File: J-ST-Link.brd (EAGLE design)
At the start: 35.6 x 25.4 mm, 17 parts, among them IC1 TLV70433

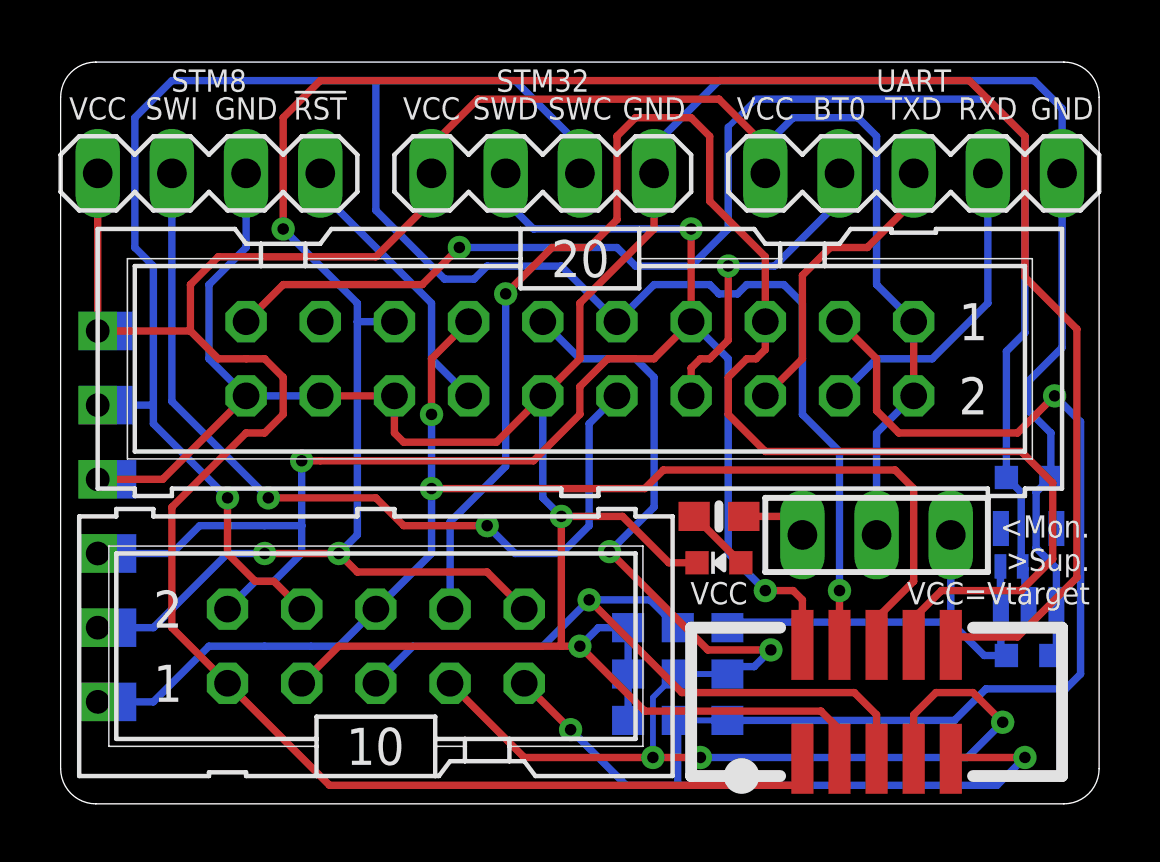
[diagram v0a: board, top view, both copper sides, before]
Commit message: Optimised routing
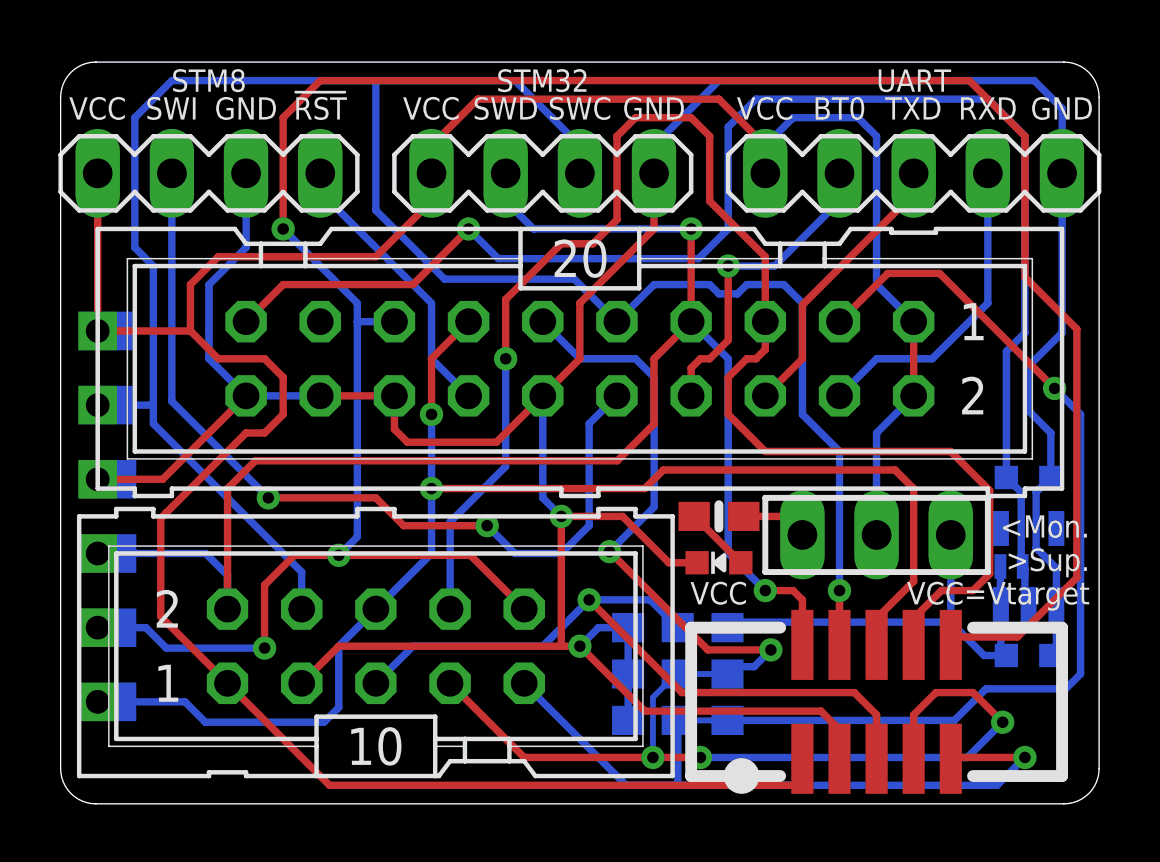
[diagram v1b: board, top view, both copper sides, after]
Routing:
- net TDI: track 55.2 -> 51.0 mm
- net !RESET: track 82.0 -> 83.8 mm
- net SWO/TDO: track 44.9 -> 46.7 mm
- net UART_TX: track 10.5 -> 9.72 mm
- net SWCLK/TCK: track 73.4 -> 72.6 mm, vias 2 -> 1
- net !TRST: track 33.2 -> 32.6 mm
- net SWDIO/TMS: track 53.8 -> 53.7 mm, vias 3 -> 2
- net TRST/NC/GND: vias 2 -> 1

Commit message: Optimised schematic
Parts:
- R1: value 1K -> 330R
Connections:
- net SWIM_RST renamed !SWIM_RST
- net VTREF renamed VCC
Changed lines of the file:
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@@
 <grid distance="0.127" unitdist="mm" unit="mm" style="dots" multiple="4" display="yes" altdistance="1" altunitdist="mil" altunit="mil"/>
 <layers>
-<layer number="1" name="Top" color="4" fill="1" visible="yes" active="yes"/>
-<layer number="16" name="Bottom" color="1" fill="1" visible="yes" active="yes"/>
-<layer number="17" name="Pads" color="2" fill="1" visible="yes" active="yes"/>
-<layer number="18" name="Vias" color="2" fill="1" visible="yes" active="yes"/>
+<layer number="1" name="Top" color="4" fill="1" visible="no" active="yes"/>
+<layer number="16" name="Bottom" color="1" fill="1" visible="no" active="yes"/>
+<layer number="17" name="Pads" color="2" fill="1" visible="no" active="yes"/>
+<layer number="18" name="Vias" color="2" fill="1" visible="no" active="yes"/>
 <layer number="19" name="Unrouted" color="6" fill="1" visible="yes" active="yes"/>
 <layer number="20" name="Dimension" color="24" fill="1" visible="yes" active="yes"/>
 <layer number="21" name="tPlace" color="7" fill="1" visible="yes" active="yes"/>
-<layer number="22" name="bPlace" color="7" fill="1" visible="yes" active="yes"/>
+<layer number="22" name="bPlace" color="7" fill="1" visible="no" active="yes"/>
 <layer number="23" name="tOrigins" color="15" fill="1" visible="yes" active="yes"/>
-<layer number="24" name="bOrigins" color="15" fill="1" visible="yes" active="yes"/>
+<layer number="24" name="bOrigins" color="15" fill="1" visible="no" active="yes"/>
 <layer number="25" name="tNames" color="7" fill="1" visible="yes" active="yes"/>
-<layer number="26" name="bNames" color="7" fill="1" visible="yes" active="yes"/>
-<layer number="27" name="tValues" color="7" fill="1" visible="yes" active="yes"/>
-<layer number="28" name="bValues" color="7" fill="1" visible="yes" active="yes"/>
-<layer number="29" name="tStop" color="7" fill="3" visible="no" active="yes"/>
+<layer number="26" name="bNames" color="7" fill="1" visible="no" active="yes"/>
+<layer number="27" name="tValues" color="7" fill="1" visible="no" active="yes"/>
+<layer number="28" name="bValues" color="7" fill="1" visible="no" active="yes"/>
+<layer number="29" name="tStop" color="7" fill="3" visible="yes" active="yes"/>
 <layer number="30" name="bStop" color="7" fill="6" visible="no" active="yes"/>
 <layer number="31" name="tCream" color="7" fill="4" visible="no" active="yes"/>
@@
 <layer number="37" name="tTest" color="7" fill="1" visible="no" active="yes"/>
 <layer number="38" name="bTest" color="7" fill="1" visible="no" active="yes"/>
-<layer number="39" name="tKeepout" color="4" fill="11" visible="yes" active="yes"/>
-<layer number="40" name="bKeepout" color="1" fill="11" visible="yes" active="yes"/>
-<layer number="41" name="tRestrict" color="4" fill="10" visible="yes" active="yes"/>
-<layer number="42" name="bRestrict" color="1" fill="10" visible="yes" active="yes"/>
-<layer number="43" name="vRestrict" color="2" fill="10" visible="yes" active="yes"/>
+<layer number="39" name="tKeepout" color="4" fill="11" visible="no" active="yes"/>
+<layer number="40" name="bKeepout" color="1" fill="11" visible="no" active="yes"/>
+<layer number="41" name="tRestrict" color="4" fill="10" visible="no" active="yes"/>
+<layer number="42" name="bRestrict" color="1" fill="10" visible="no" active="yes"/>
+<layer number="43" name="vRestrict" color="2" fill="10" visible="no" active="yes"/>
 <layer number="44" name="Drills" color="7" fill="1" visible="no" active="yes"/>
-<layer number="45" name="Holes" color="7" fill="1" visible="no" active="yes"/>
-<layer number="46" name="Milling" color="3" fill="1" visible="no" active="yes"/>
-<layer number="47" name="Measures" color="7" fill="1" visible="no" active="yes"/>
+<layer number="45" name="Holes" color="7" fill="1" visible="yes" active="yes"/>
+<layer number="46" name="Milling" color="3" fill="1" visible="yes" active="yes"/>
+<layer number="47" name="Measures" color="7" fill="1" visible="yes" active="yes"/>
 <layer number="48" name="Document" color="7" fill="1" visible="yes" active="yes"/>
 <layer number="49" name="Reference" color="7" fill="1" visible="yes" active="yes"/>
-<layer number="51" name="tDocu" color="7" fill="1" visible="yes" active="yes"/>
-<layer number="52" name="bDocu" color="7" fill="1" visible="yes" active="yes"/>
+<layer number="51" name="tDocu" color="7" fill="1" visible="no" active="yes"/>
+<layer number="52" name="bDocu" color="7" fill="1" visible="no" active="yes"/>
 <layer number="88" name="SimResults" color="9" fill="1" visible="no" active="no"/>
 <layer number="89" name="SimProbes" color="9" fill="1" visible="no" active="no"/>
@@
 </element>
 <element name="10-127" library="Progger2 (3)" package="CON-HARTING-ML_ML10S" value="" x="27.94" y="3.4925" smashed="yes"/>
-<element name="R1" library="microbuilder" package="0603-NO" value="1K" x="22.5425" y="9.8425" smashed="yes"/>
+<element name="R1" library="microbuilder" package="0603-NO" value="330R" x="22.5425" y="9.8425" smashed="yes"/>
 <element name="LED1" library="microbuilder" package="CHIPLED_0603_NOOUTLINE" value="" x="22.5425" y="8.255" smashed="yes" rot="R90">
 <attribute name="VALUE" x="24.5425" y="7.255" size="1.27" layer="27" rot="R90"/>
@@
 </elements>
 <signals>
-<signal name="VTREF">
+<signal name="VCC">
 <contactref element="J-/ST-LINK" pad="1"/>
 <contactref element="J-/ST-LINK" pad="2"/>
@@
 <wire x1="10.795" y1="10.4775" x2="7.112" y2="10.4775" width="0.254" layer="1"/>
 </signal>
-<signal name="SWIM_RST">
+<signal name="!SWIM_RST">
 <contactref element="STM8" pad="4"/>
 <contactref element="J-/ST-LINK" pad="14"/>
